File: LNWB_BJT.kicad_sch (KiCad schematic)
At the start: 107 parts, among them J1 Input, J2 wire2board, J3 Input, J4 wire2board, Q1 2N4401, Q2 2N4401, Q3 2N3906, Q4 BD679, Q5 BD680, U1 TL072, U2 AD8039, U3 AD8009, U4 AD8009

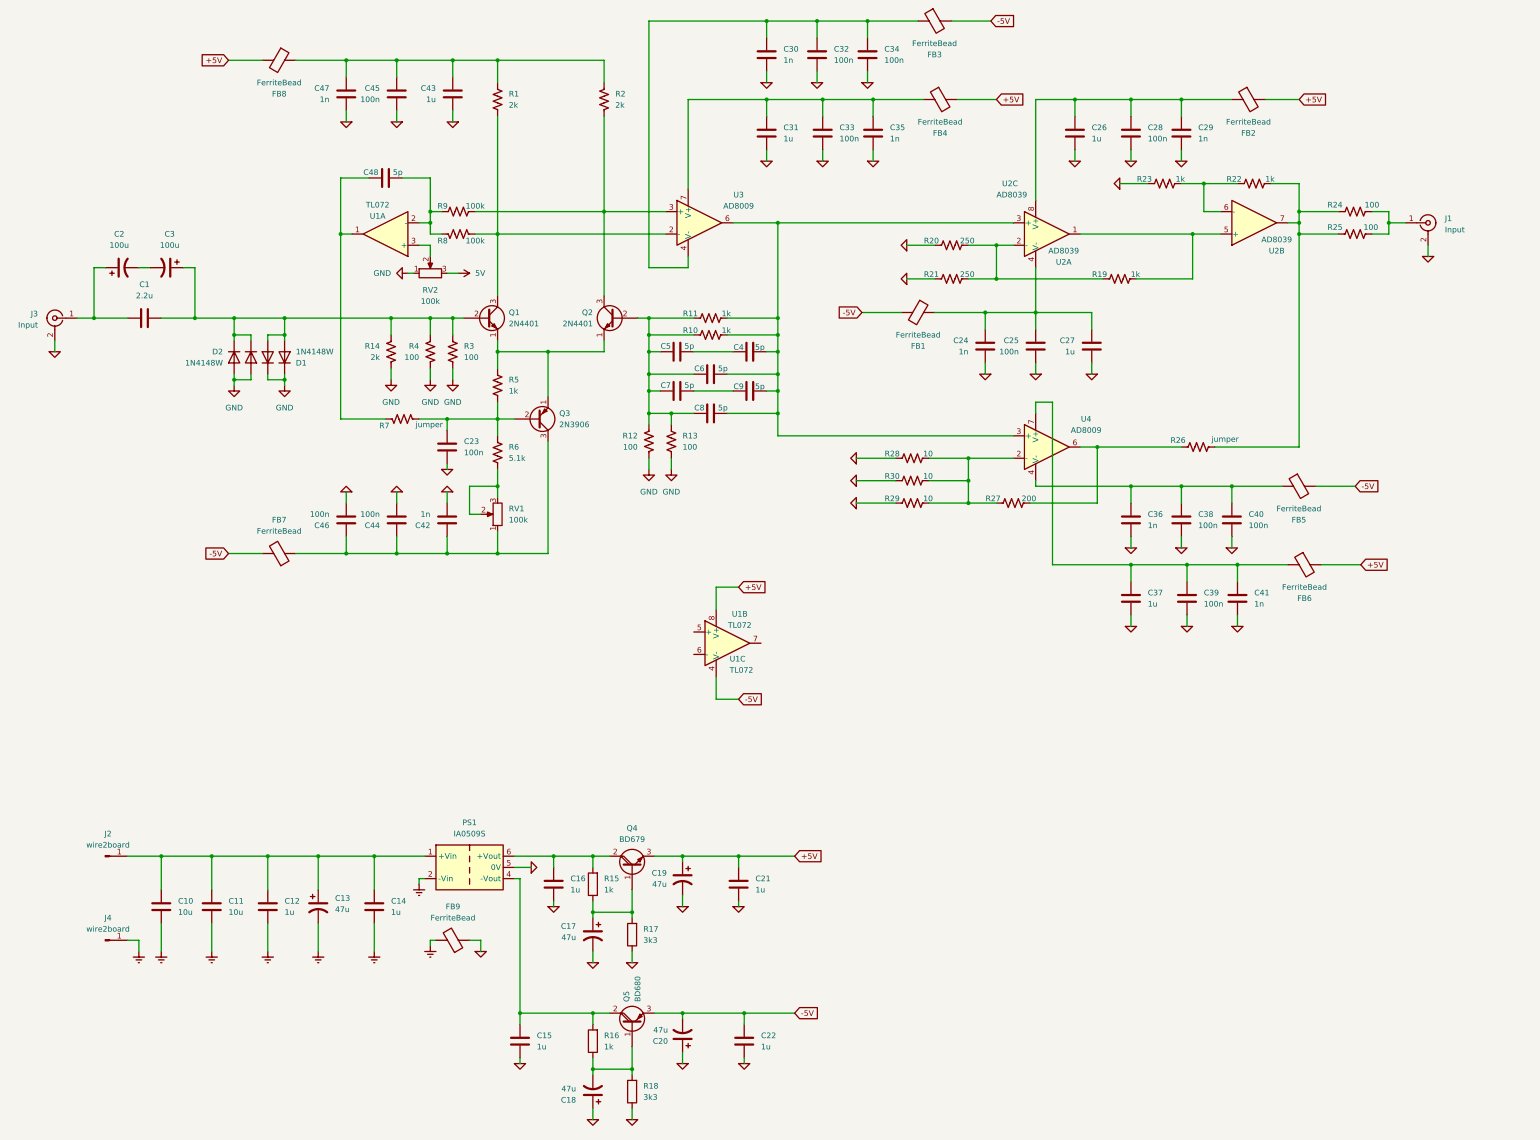
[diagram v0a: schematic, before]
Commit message: Mounting holes, edge cuts.
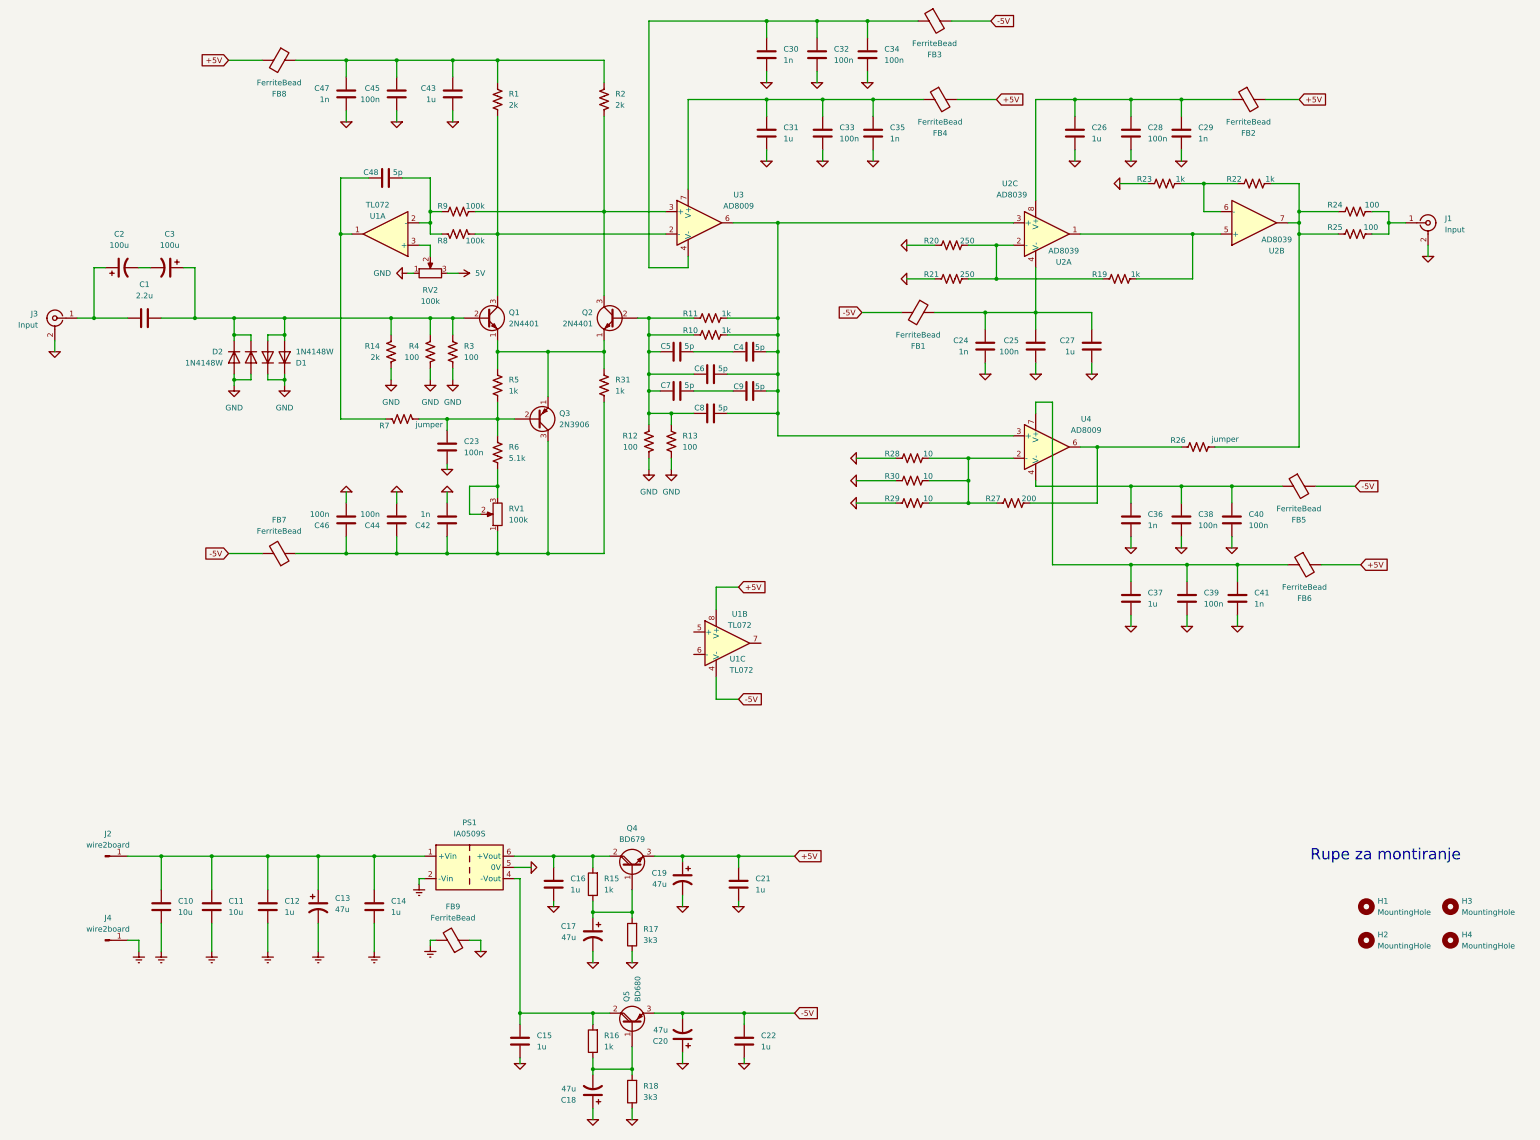
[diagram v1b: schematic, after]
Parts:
- added H1, H2, H3, H4: MountingHole, MountingHole:MountingHole_3.2mm_M3_ISO14580_Pad_TopBottom, symbol Mechanical:MountingHole
- added R31: 1k, Resistor_SMD:R_0603_1608Metric_Pad0.98x0.95mm_HandSolder, symbol Device:R_US
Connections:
- net at C42.2, C44.2, C46.2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: now also R31.2
- net at Q1.1 (E), Q2.1 (E), Q3.1 (E)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: now also R31.1
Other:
- note added: "Rupe za montiranje"

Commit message: klfdsa.wq
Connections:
- net 0: no longer C15.2, C16.2, C17.2, C18.1, C19.2, C20.1, C21.2, C22.2, C23.2, C26.1, C28.1, C29.1, C30.1, C31.1, C32.1, C33.1, C34.1, C35.1, C36.1, C37.1, C38.1, C39.1, C40.1, C41.1, C42.1, C43.1, C44.1, C45.1, C46.1, C47.1, J3.2 (Ext), PS1.5 (0V), R17.1, R18.1
- net GND: now also C15.2, C16.2, C17.2, C18.1, C19.2, C20.1, C21.2, C22.2, C23.2, C26.1, C28.1, C29.1, C30.1, C31.1, C32.1, C33.1, C34.1, C35.1, C36.1, C37.1, C38.1, C39.1, C40.1, C41.1, C42.1, C43.1, C44.1, C45.1, C46.1, C47.1, J3.2 (Ext), PS1.5 (0V), R17.1, R18.1
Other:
- moved on the sheet: C22, C28, C29, C33, C35, C39, C41, C43

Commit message: send.
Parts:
- added C49, C50: 100n, Resistor_SMD:R_0603_1608Metric_Pad0.98x0.95mm_HandSolder, symbol Device:C
- added D5: 1N4148, Diode_THT:D_DO-35_SOD27_P7.62mm_Horizontal, symbol Diode:1N4148
- added R32: 100k, Resistor_SMD:R_0603_1608Metric_Pad0.98x0.95mm_HandSolder, symbol Device:R_US
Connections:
- net +5V: now also C50.2, R32.2
- net -5V: now also C49.2
- net 0: no longer C24.1, C25.1, C27.1, J1.2 (Ext), R20.1, R21.1, R23.1, R28.1, R29.1, R30.1
- net GND: now also C24.1, C25.1, C27.1, J1.2 (Ext), R20.1, R21.1, R23.1, R28.1, R29.1, R30.1, U1.6 (-), C49.1, C50.1, D5.1 (K)
- net at U1.5 (+): now also D5.2 (A), R32.1
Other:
- moved on the sheet: C27

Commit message: PCB.
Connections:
- net 0 is gone; now on net GND: FB9.1
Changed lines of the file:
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@@
 	)
 	(symbol
+		(lib_id "power:GND")
+		(at 129.54 238.76 0)
+		(mirror y)
+		(unit 1)
+		(exclude_from_sim no)
+		(in_bom yes)
+		(on_board yes)
+		(dnp no)
+		(property "Reference" "#PWR065"
+			(at 129.54 245.11 0)
+			(effects
+				(font
+					(size 1.27 1.27)
+				)
+				(hide yes)
+			)
+		)
+		(property "Value" "GND"
+			(at 132.588 239.268 0)
+			(effects
+				(font
+					(size 1.27 1.27)
+				)
+			)
+		)
+		(property "Footprint" ""
+			(at 129.54 238.76 0)
+			(effects
+				(font
+					(size 1.27 1.27)
+				)
+				(hide yes)
+			)
+		)
+		(property "Datasheet" ""
+			(at 129.54 238.76 0)
+			(effects
+				(font
+					(size 1.27 1.27)
+				)
+				(hide yes)
+			)
+		)
+		(property "Description" "Power symbol creates a global label with name \"GND\" , ground"
+			(at 129.54 238.76 0)
+			(effects
+				(font
+					(size 1.27 1.27)
+				)
+				(hide yes)
+			)
+		)
+		(pin "1"
+		)
+		(instances
+			(project "LNWB_BJT"
+				(path "/8a55cab2-ac90-40a0-8f8e-219f66b3018a"
+					(reference "#PWR065")
+					(unit 1)
+				)
+			)
+		)
+	)
+	(symbol
 		(lib_id "Device:R_US")
 		(at 327.66 71.12 90)
@@
 					(unit 1)
 				)
-			)
-		)
-	)
-	(symbol
-		(lib_id "Simulation_SPICE:0")
-		(at 129.54 238.76 0)
-		(unit 1)
-		(exclude_from_sim no)
-		(in_bom yes)
-		(on_board yes)
-		(dnp no)
-		(fields_autoplaced yes)
-		(property "Reference" "#GND045"
-			(at 129.54 241.3 0)
-			(effects
-				(font
-					(size 1.27 1.27)
-				)
-				(hide yes)
-			)
-		)
-		(property "Value" "0"
-			(at 129.54 236.22 0)
-			(effects
-				(font
-					(size 1.27 1.27)
-				)
-				(hide yes)
-			)
-		)
-		(property "Footprint" ""
-			(at 129.54 238.76 0)
-			(effects
-				(font
-					(size 1.27 1.27)
-				)
-				(hide yes)
-			)
-		)
-		(property "Datasheet" "~"
-			(at 129.54 238.76 0)
-			(effects
-				(font
-					(size 1.27 1.27)
-				)
-				(hide yes)
-			)
-		)
-		(property "Description" ""
-			(at 129.54 238.76 0)
-			(effects
-				(font
-					(size 1.27 1.27)
-				)
-				(hide yes)
-			)
-		)
-		(pin "1"
-		)
-		(instances
-			(project "LNWB_BJT"
-				(path "/8a55cab2-ac90-40a0-8f8e-219f66b3018a"
-					(reference "#GND045")
-					(unit 1)
-				)
